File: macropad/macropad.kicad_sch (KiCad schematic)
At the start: 44 parts, among them IC1 W25Q16JVUXIQ_TR, J1 Conn_01x03_Female, J2 USB_C_Receptacle, SW1 BOOT, SW2 RESET, U1 RP2040, U10 DRV5057A3, U11 DRV5057A3, U12 OLED_256x64_I2C, U2 DRV5057A3, U3 DRV5057A3, U4 DRV5057A3, U5 DRV5057A3, U6 CD74HC4067SM96E4, U7 DRV5057A3, U8 DRV5057A3, U9 NCP1117-3.3_SOT223, Y1 ABLS-12.000MHZ-B4-T

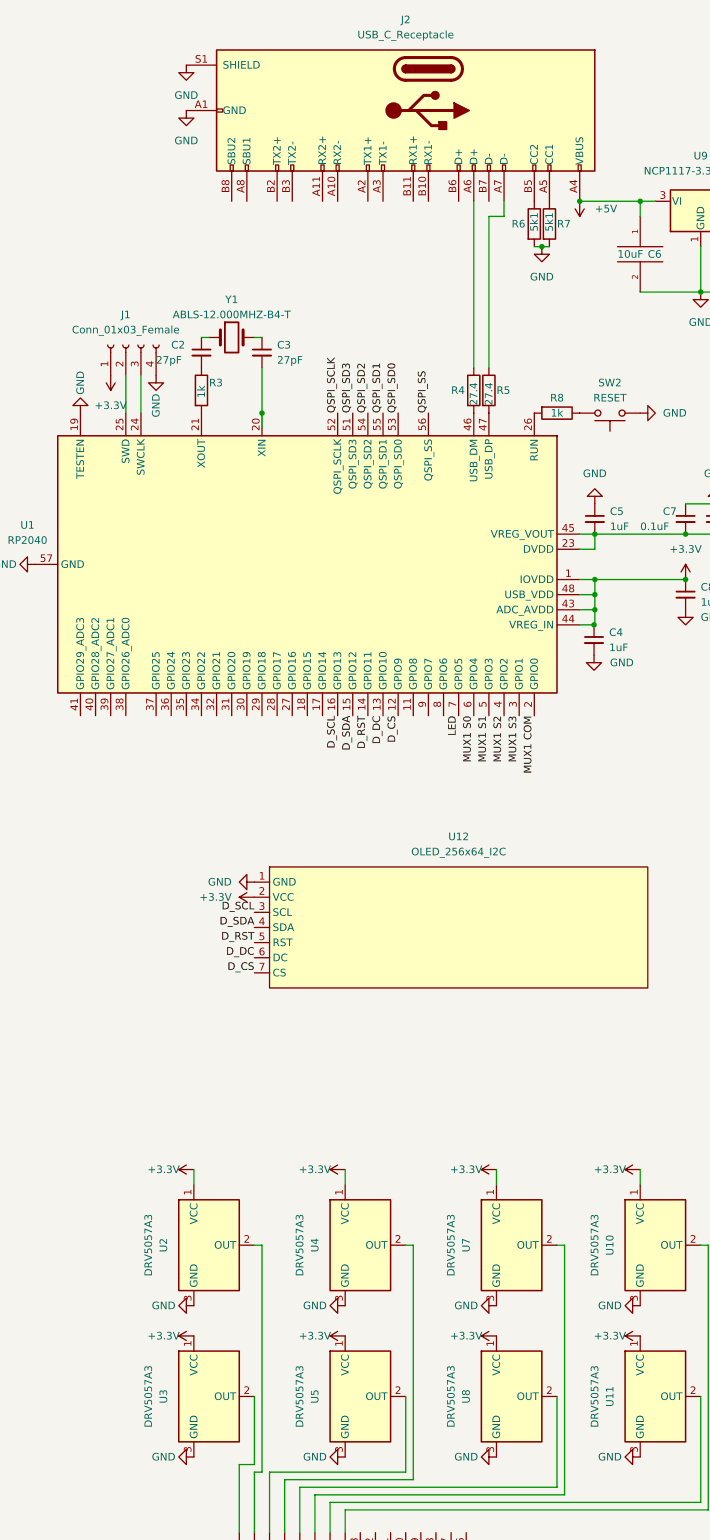
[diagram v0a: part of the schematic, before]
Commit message: fix multiple issues with macropad pcb
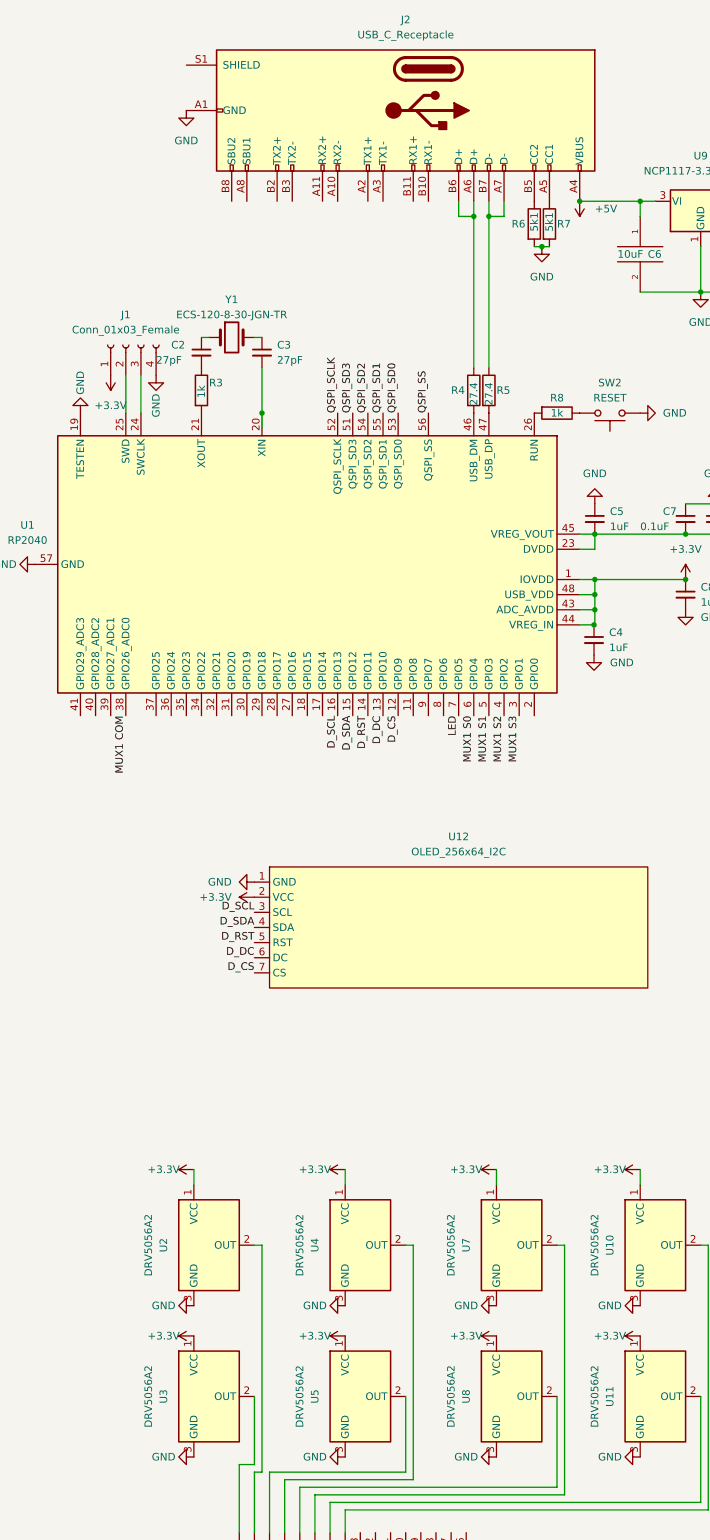
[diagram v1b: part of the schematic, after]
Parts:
- C1, C7, C9: MPN (none) -> MSAST105SB7104KFNB25
- C11, C6: MPN (none) -> GRM155R60J106ME15D
- C2, C3: MPN (none) -> GJM1555C1H270FB01D
- C4, C5, C8: MPN (none) -> MAASA105CD7105KFCA01
- J2: MPN 12401610E4#2A -> 12401832E402A
- LED2, LED4, LED6, LED8: footprint lib:LED_MX_SK6812MINI-R -> lib:LED_MX_SK6812MINI-R_FLIPPED
- R1, R3, R8: MPN (none) -> RCC06031K00FKEA
- R2: MPN (none) -> ERJ-3EKF1002V
- R4, R5: MPN (none) -> CRCW060327R4FKEB
- R6, R7: MPN (none) -> ERJ-3EKF5101V
- U10, U11, U2, U3, U4, U5, U7, U8: value DRV5057A3 -> DRV5056A2; footprint lib:DRV5057A3_K -> lib:DRV505x; MPN DRV5057A3QDBZT -> DRV5056A2QDBZT
- Y1: value ABLS-12.000MHZ-B4-T -> ECS-120-8-30-JGN-TR
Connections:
- net GND: no longer J2.S1 (SHIELD)
- net MUX1 COM: now also U1.38 (GPIO26_ADC0); no longer U1.2 (GPIO0)
- net at J2.A6 (D+), R4.1: now also J2.B6 (D+)
- net at J2.A7 (D-), R5.1: now also J2.B7 (D-)

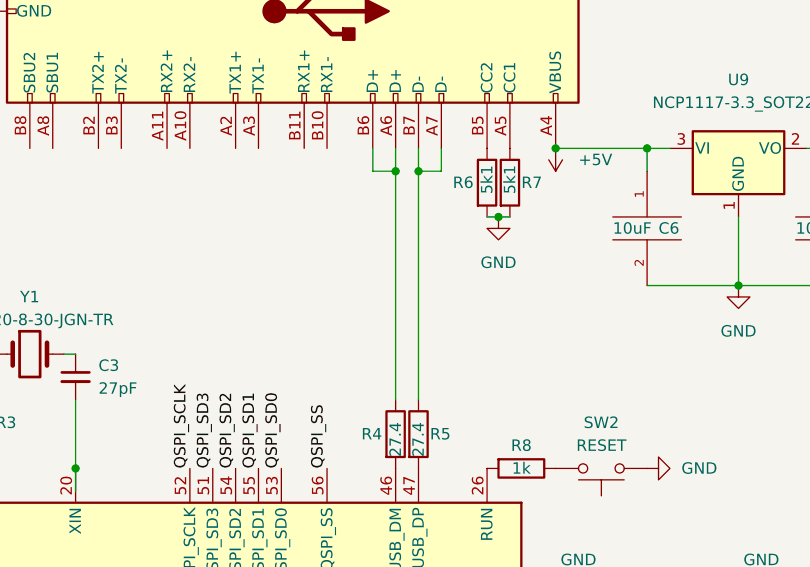
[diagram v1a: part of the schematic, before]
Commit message: flip usb data lines to correct orientation
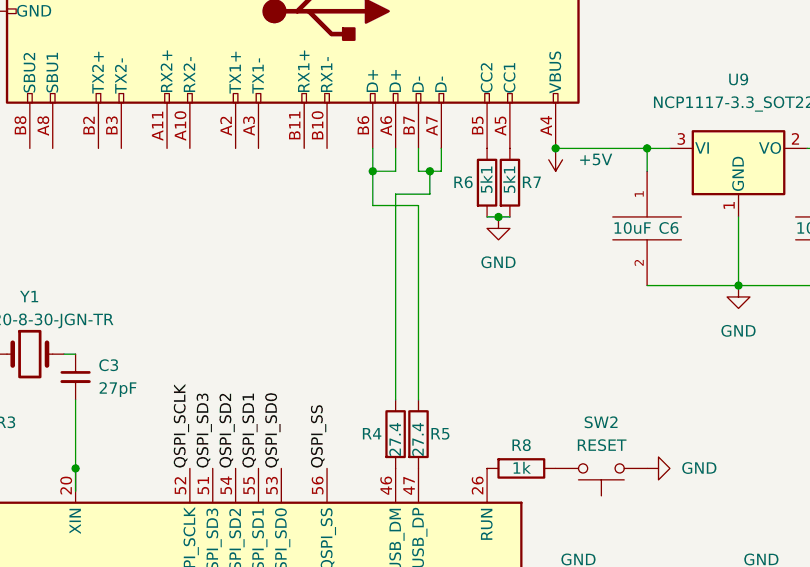
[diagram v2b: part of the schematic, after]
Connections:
- net at J2.A6 (D+), J2.B6 (D+): now also R5.1; no longer R4.1
- net at J2.A7 (D-), J2.B7 (D-): now also R4.1; no longer R5.1
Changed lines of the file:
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@@
   (junction (at 62.23 71.12) (diameter 0) (color 0 0 0 0)
   )
+  (junction (at 167.64 55.88) (diameter 0) (color 0 0 0 0)
+  )
   (junction (at 273.05 236.22) (diameter 0) (color 0 0 0 0)
   )
@@
   (junction (at 297.18 255.27) (diameter 0) (color 0 0 0 0)
   )
-  (junction (at 170.18 55.88) (diameter 0) (color 0 0 0 0)
-  )
   (junction (at 222.25 236.22) (diameter 0) (color 0 0 0 0)
   )
@@
   (junction (at 247.65 236.22) (diameter 0) (color 0 0 0 0)
   )
-  (junction (at 172.72 55.88) (diameter 0) (color 0 0 0 0)
+  (junction (at 173.99 55.88) (diameter 0) (color 0 0 0 0)
   )
   (junction (at 222.25 220.98) (diameter 0) (color 0 0 0 0)
@@
     (stroke (width 0) (type default))
   )
+  (wire (pts (xy 170.18 81.28) (xy 170.18 58.42))
+    (stroke (width 0) (type default))
+  )
   (wire (pts (xy 190.3657 124.46) (xy 190.5 124.46))
     (stroke (width 0) (type default))
@@
     (stroke (width 0) (type default))
   )
+  (wire (pts (xy 170.18 58.42) (xy 173.99 58.42))
+    (stroke (width 0) (type default))
+  )
   (wire (pts (xy 135.89 266.7) (xy 135.89 276.86))
     (stroke (width 0) (type default))
@@
     (stroke (width 0) (type default))
   )
+  (wire (pts (xy 173.99 55.88) (xy 172.72 55.88))
+    (stroke (width 0) (type default))
+  )
   (wire (pts (xy 190.5 109.22) (xy 190.5 111.76))
     (stroke (width 0) (type default))
@@
     (stroke (width 0) (type default))
   )
+  (wire (pts (xy 172.72 81.28) (xy 172.72 59.69))
+    (stroke (width 0) (type default))
+  )
   (wire (pts (xy 148.59 276.86) (xy 148.59 273.05))
     (stroke (width 0) (type default))
@@
     (stroke (width 0) (type default))
   )
+  (wire (pts (xy 167.64 59.69) (xy 167.64 55.88))
+    (stroke (width 0) (type default))
+  )
   (wire (pts (xy 175.26 53.34) (xy 175.26 55.88))
     (stroke (width 0) (type default))
@@
     (stroke (width 0) (type default))
   )
-  (wire (pts (xy 175.26 55.88) (xy 172.72 55.88))
+  (wire (pts (xy 175.26 55.88) (xy 173.99 55.88))
     (stroke (width 0) (type default))
   )
@@
     (stroke (width 0) (type default))
   )
+  (wire (pts (xy 173.99 58.42) (xy 173.99 55.88))
+    (stroke (width 0) (type default))
+  )
   (wire (pts (xy 208.28 254) (xy 208.28 271.78))
     (stroke (width 0) (type default))
@@
     (stroke (width 0) (type default))
   )
+  (wire (pts (xy 172.72 59.69) (xy 167.64 59.69))
+    (stroke (width 0) (type default))
+  )
   (wire (pts (xy 190.5 111.76) (xy 187.96 111.76))
     (stroke (width 0) (type default))
@@
     (stroke (width 0) (type default))
   )
-  (wire (pts (xy 172.72 55.88) (xy 172.72 81.28))
-    (stroke (width 0) (type default))
-  )
   (wire (pts (xy 209.55 273.05) (xy 209.55 228.6))
     (stroke (width 0) (type default))
@@
     (stroke (width 0) (type default))
   )
-  (wire (pts (xy 170.18 55.88) (xy 170.18 81.28))
-    (stroke (width 0) (type default))
-  )
